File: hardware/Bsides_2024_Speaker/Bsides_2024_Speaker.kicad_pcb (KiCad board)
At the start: 2 copper layers, 144.4 x 144.3 mm, 65 parts, among them J1 Add_On, J2 Battery, J3 Battery, J4 OLED, J5 Serial_IN, J6 Serial_OUT, P1 USB_C_Plug_USB2.0, Q1 DMG3415U-7, SW1 ON, SW2 SW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

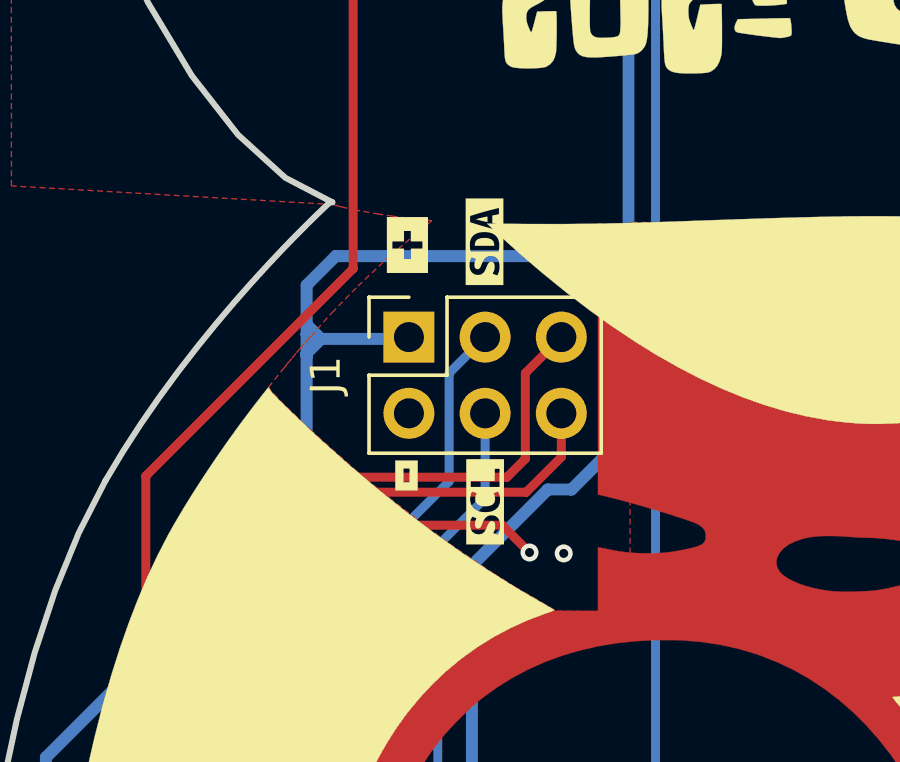
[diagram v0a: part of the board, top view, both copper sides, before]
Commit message: feat(hw): add labels and logos speaker
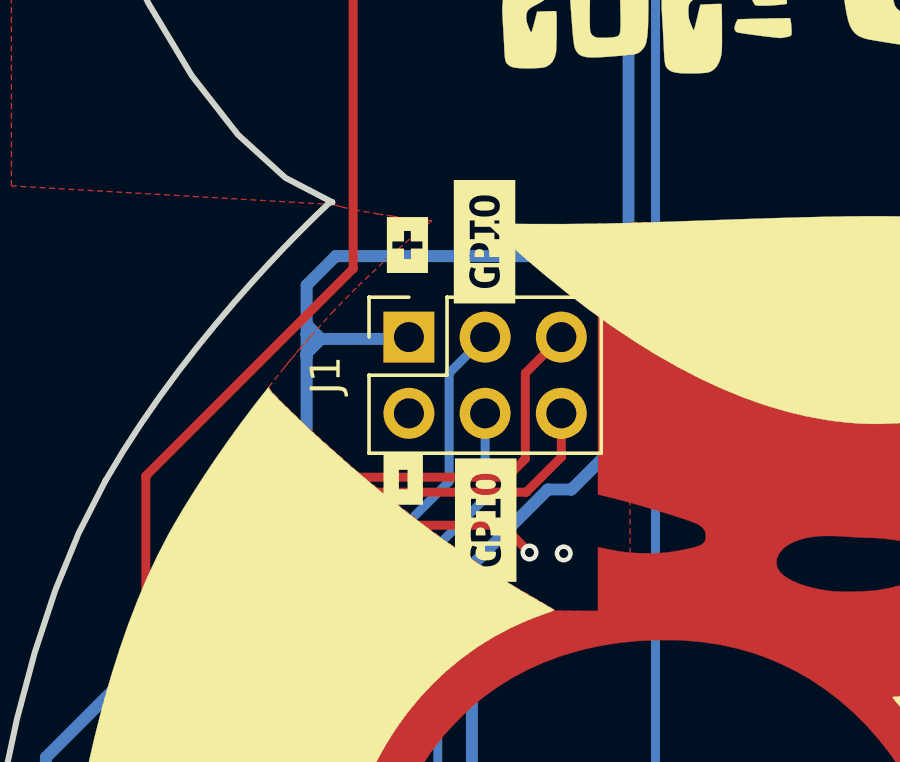
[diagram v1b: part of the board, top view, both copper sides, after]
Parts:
- removed the kibuzzard-666B5BCA at (154.1, 47.2)
- removed kibuzzard-666B5C0A (x2): G***, kibuzzard-666B5C0A
- removed kibuzzard-666B5C24: G***, kibuzzard-666B5C24
- removed kibuzzard-666B5C33: G***, kibuzzard-666B5C33
- added G***: LOGO, LOGO, B.Cu at (150.9, 112.1)
- added G***: LOGO, LOGO, B.Cu at (170.9, 124.2)
- added REF**: OSHW-Logo_7.5x8mm_SilkScreen, Symbol:OSHW-Logo_7.5x8mm_SilkScreen, B.Cu at (97.6, 142.1)
- added kibuzzard-666C89F7: G***, kibuzzard-666C89F7, B.Cu at (137.3, 47.2)
- added kibuzzard-666C8A00: G***, kibuzzard-666C8A00, B.Cu at (154.1, 47.2)
- added kibuzzard-666C8A1B: G***, kibuzzard-666C8A1B, F.Cu at (124.3, 68.7)
- added kibuzzard-666C8A24: G***, kibuzzard-666C8A24, F.Cu at (124.3, 78.0)
- added kibuzzard-666C8A46: G***, kibuzzard-666C8A46, F.Cu at (121.6, 76.6)
- added kibuzzard-666C8E87: G***, kibuzzard-666C8E87, B.Cu at (151.0, 107.9)
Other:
- board text added: "4e6576657220676f6e6e612067 69766520796f752075700a4e65 76657220676f6e6e61206c6574 20796f7520646f776e0a4e6576 657220676f6e6e612072756e20 61726f756e6420616e64206465 7365727420796f75"
- board text added: "Aqui inicia el tour por latinoamerica Parce Wey Che"
- board text added: "Elige tu bando, rudo o tecnico?"
- board text added: "Lucharan de 2 a 3 caidas sin limite de tiempo!!"
